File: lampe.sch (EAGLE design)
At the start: 29 parts, among them SW1 SWITCH, SW2 SWITCH, SW3 SWITCH, SW4 SWITCH, T3 LTR-4206, X1 USBPCB

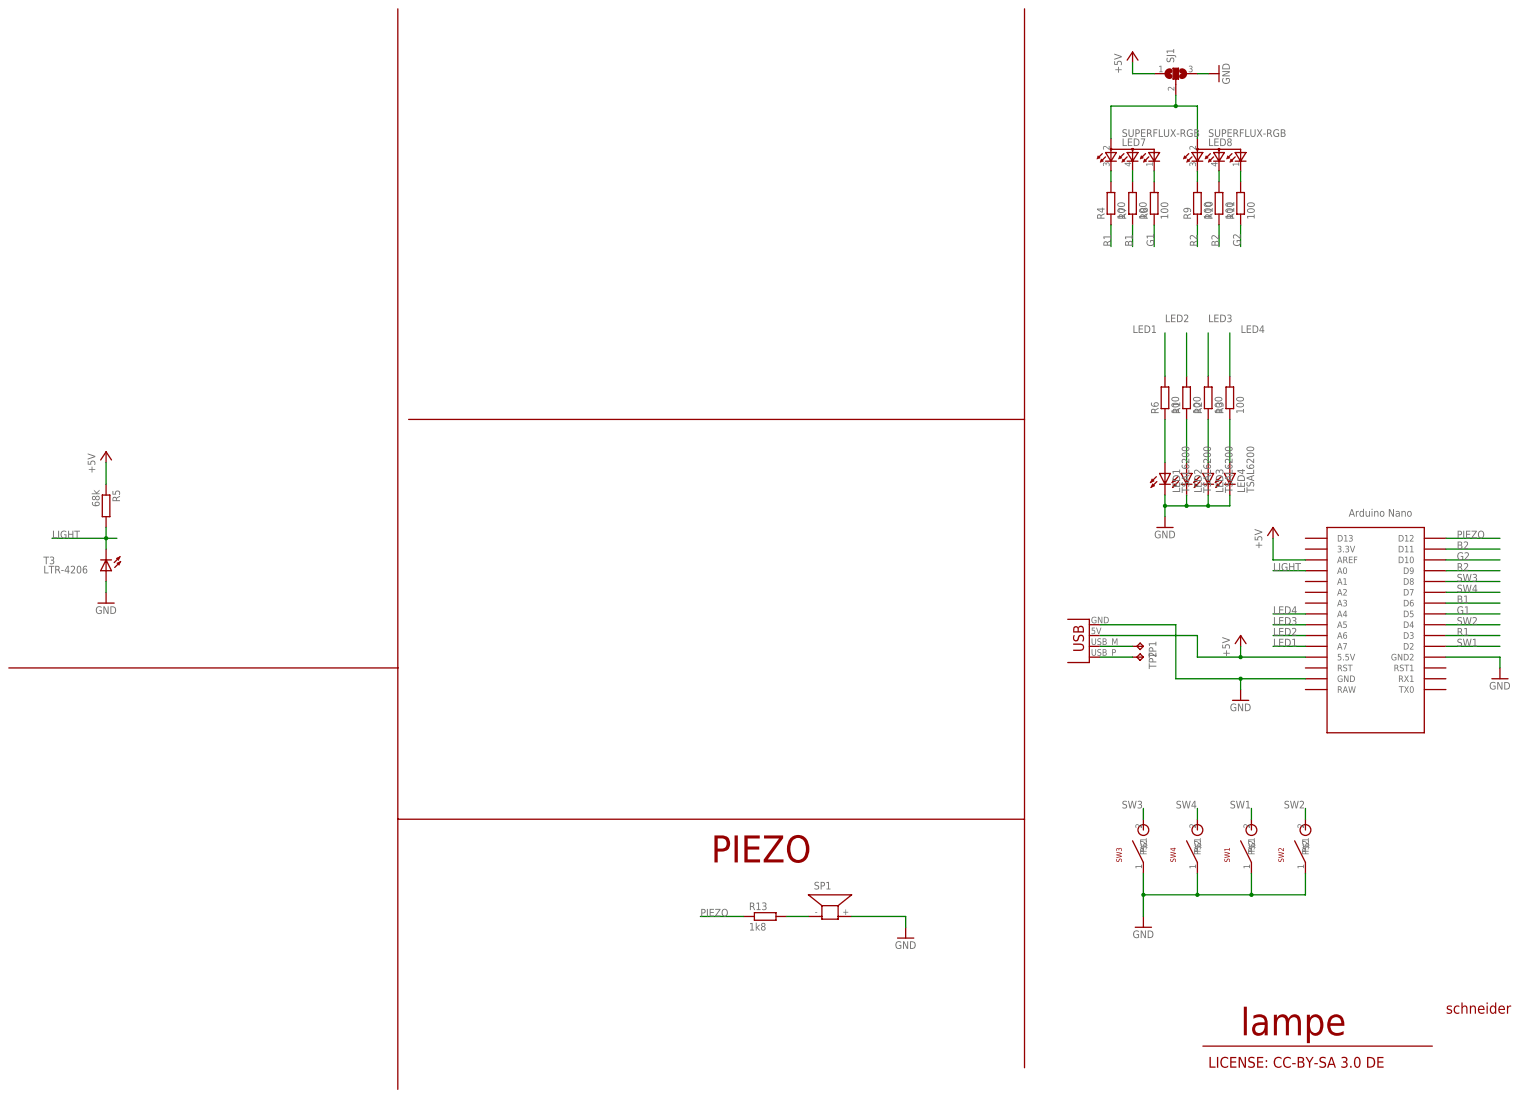
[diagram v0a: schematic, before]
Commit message: feat(lampe): Fix silk screen and some values
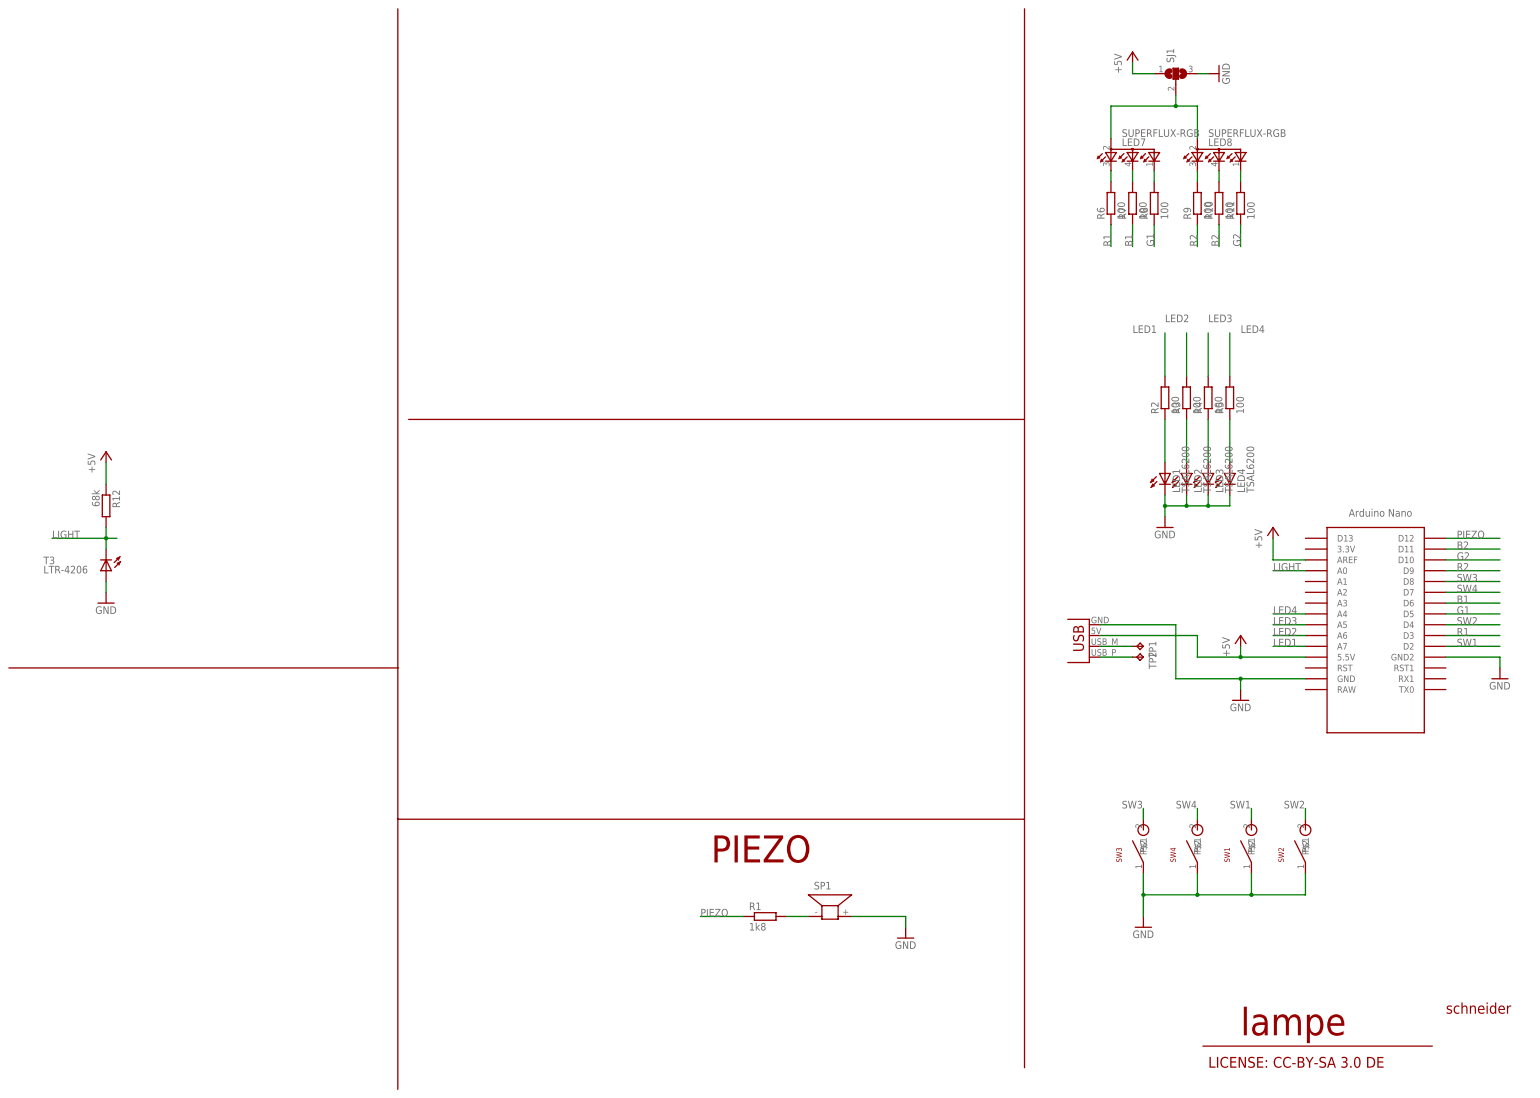
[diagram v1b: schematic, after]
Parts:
- removed R13: 1k8, rcl:R-EU_0207/7
- added R12: 68k, rcl:R-EU_0207/7
- R1: value 100 -> 1k8
- R5: value 68k -> 100
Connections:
- net +5V: now also R12.1; no longer R5.1
- net LED1: now also R2.2; no longer R6.2
- net LED2: now also R3.2; no longer R1.2
- net LED3: now also R4.2; no longer R2.2
- net LED4: now also R5.2; no longer R3.2
- net LIGHT: now also R12.2; no longer R5.2
- net N$1: now also R3.1; no longer R1.1
- net N$10: now also R5.1; no longer R3.1
- net N$17: now also R2.1; no longer R6.1
- net N$2: now also R6.2; no longer R4.2
- net N$29: now also R1.2; no longer R13.2
- net N$3: now also R4.1; no longer R2.1
- net PIEZO: now also R1.1; no longer R13.1
- net R1: now also R6.1; no longer R4.1
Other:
- moved on the sheet: R1, R2, R3, R4, R5, R6
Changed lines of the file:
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@@
 <parts>
 <part name="T3" library="led" deviceset="LED" device="3MM" value="LTR-4206"/>
-<part name="R5" library="rcl" deviceset="R-EU_" device="0207/7" value="68k"/>
+<part name="R12" library="rcl" deviceset="R-EU_" device="0207/7" value="68k"/>
 <part name="GND1" library="supply1" deviceset="GND" device=""/>
 <part name="GND6" library="supply1" deviceset="GND" device=""/>
@@
 <part name="GND10" library="supply1" deviceset="GND" device=""/>
 <part name="LED1" library="led" deviceset="LED" device="5MM" value="TSAL6200"/>
-<part name="R6" library="rcl" deviceset="R-EU_" device="0207/7" value="100"/>
-<part name="R13" library="rcl" deviceset="R-EU_" device="0207/7" value="1k8"/>
+<part name="R2" library="rcl" deviceset="R-EU_" device="0207/7" value="100"/>
+<part name="R1" library="rcl" deviceset="R-EU_" device="0207/7" value="1k8"/>
 <part name="GND13" library="supply1" deviceset="GND" device=""/>
 <part name="SW4" library="badge" deviceset="SWITCH" device="" value=""/>
@@
 <part name="SW1" library="badge" deviceset="SWITCH" device="" value=""/>
 <part name="SW2" library="badge" deviceset="SWITCH" device="" value=""/>
-<part name="R1" library="rcl" deviceset="R-EU_" device="0207/7" value="100"/>
-<part name="R2" library="rcl" deviceset="R-EU_" device="0207/7" value="100"/>
 <part name="R3" library="rcl" deviceset="R-EU_" device="0207/7" value="100"/>
 <part name="R4" library="rcl" deviceset="R-EU_" device="0207/7" value="100"/>
+<part name="R5" library="rcl" deviceset="R-EU_" device="0207/7" value="100"/>
+<part name="R6" library="rcl" deviceset="R-EU_" device="0207/7" value="100"/>
 <part name="R7" library="rcl" deviceset="R-EU_" device="0207/7" value="100"/>
 <part name="R8" library="rcl" deviceset="R-EU_" device="0207/7" value="100"/>
@@
 <attribute name="VALUE" x="15.748" y="123.825" size="1.778" layer="96"/>
 </instance>
-<instance part="R5" gate="G$1" x="30.48" y="139.7" rot="R270"/>
+<instance part="R12" gate="G$1" x="30.48" y="139.7" rot="R270"/>
 <instance part="GND1" gate="1" x="274.32" y="40.64"/>
 <instance part="GND6" gate="1" x="30.48" y="116.84"/>
@@
 <instance part="GND10" gate="1" x="218.44" y="38.1"/>
 <instance part="LED1" gate="G$1" x="279.4" y="147.32"/>
-<instance part="R6" gate="G$1" x="279.4" y="165.1" rot="R90"/>
-<instance part="R13" gate="G$1" x="185.42" y="43.18"/>
+<instance part="R2" gate="G$1" x="279.4" y="165.1" rot="R90"/>
+<instance part="R1" gate="G$1" x="185.42" y="43.18"/>
 <instance part="GND13" gate="1" x="279.4" y="134.62"/>
 <instance part="SW4" gate="G$1" x="287.02" y="58.42" rot="R90"/>
@@
 <instance part="SW1" gate="G$1" x="299.72" y="58.42" rot="R90"/>
 <instance part="SW2" gate="G$1" x="312.42" y="58.42" rot="R90"/>
-<instance part="R1" gate="G$1" x="284.48" y="165.1" rot="R90"/>
-<instance part="R2" gate="G$1" x="289.56" y="165.1" rot="R90"/>
-<instance part="R3" gate="G$1" x="294.64" y="165.1" rot="R90"/>
-<instance part="R4" gate="G$1" x="266.7" y="210.82" rot="R90"/>
+<instance part="R3" gate="G$1" x="284.48" y="165.1" rot="R90"/>
+<instance part="R4" gate="G$1" x="289.56" y="165.1" rot="R90"/>
+<instance part="R5" gate="G$1" x="294.64" y="165.1" rot="R90"/>
+<instance part="R6" gate="G$1" x="266.7" y="210.82" rot="R90"/>
 <instance part="R7" gate="G$1" x="271.78" y="210.82" rot="R90"/>
 <instance part="R8" gate="G$1" x="276.86" y="210.82" rot="R90"/>
@@
 <net name="N$29" class="0">
 <segment>
-<pinref part="R13" gate="G$1" pin="2"/>
+<pinref part="R1" gate="G$1" pin="2"/>
 <wire x1="190.5" y1="43.18" x2="195.58" y2="43.18" width="0.1524" layer="91"/>
 <pinref part="SP1" gate="G$1" pin="1"/>
@@
 <segment>
 <wire x1="279.4" y1="160.02" x2="279.4" y2="149.86" width="0.1524" layer="91"/>
-<pinref part="R6" gate="G$1" pin="1"/>
+<pinref part="R2" gate="G$1" pin="1"/>
 <pinref part="LED1" gate="G$1" pin="A"/>
 </segment>
@@
 <wire x1="180.34" y1="43.18" x2="170.18" y2="43.18" width="0.1524" layer="91"/>
 <label x="170.18" y="43.18" size="1.778" layer="95"/>
-<pinref part="R13" gate="G$1" pin="1"/>
+<pinref part="R1" gate="G$1" pin="1"/>
 </segment>
 <segment>
@@
 <wire x1="279.4" y1="170.18" x2="279.4" y2="180.34" width="0.1524" layer="91"/>
 <label x="271.78" y="180.34" size="1.778" layer="95"/>
-<pinref part="R6" gate="G$1" pin="2"/>
+<pinref part="R2" gate="G$1" pin="2"/>
 </segment>
 <segment>
@@
 <junction x="30.48" y="132.08"/>
 <label x="17.78" y="132.08" size="1.778" layer="95"/>
-<pinref part="R5" gate="G$1" pin="2"/>
+<pinref part="R12" gate="G$1" pin="2"/>
 <pinref part="T3" gate="G$1" pin="C"/>
 </segment>
@@
 <net name="N$2" class="0">
 <segment>
-<pinref part="R4" gate="G$1" pin="2"/>
+<pinref part="R6" gate="G$1" pin="2"/>
 <pinref part="LED7" gate="G$1" pin="CRED"/>
 <wire x1="266.7" y1="215.9" x2="266.7" y2="218.44" width="0.1524" layer="91"/>
@@
 <segment>
 <wire x1="30.48" y1="149.86" x2="30.48" y2="144.78" width="0.1524" layer="91"/>
-<pinref part="R5" gate="G$1" pin="1"/>
+<pinref part="R12" gate="G$1" pin="1"/>
 <pinref part="P+4" gate="1" pin="+5V"/>
 </segment>
@@
 <net name="R1" class="0">
 <segment>
-<pinref part="R4" gate="G$1" pin="1"/>
+<pinref part="R6" gate="G$1" pin="1"/>
 <wire x1="266.7" y1="205.74" x2="266.7" y2="200.66" width="0.1524" layer="91"/>
 <label x="266.7" y="200.66" size="1.778" layer="95" rot="R90"/>
@@
 <segment>
 <pinref part="LED2" gate="G$1" pin="A"/>
-<pinref part="R1" gate="G$1" pin="1"/>
+<pinref part="R3" gate="G$1" pin="1"/>
 <wire x1="284.48" y1="149.86" x2="284.48" y2="160.02" width="0.1524" layer="91"/>
 </segment>
@@
 <segment>
 <pinref part="LED3" gate="G$1" pin="A"/>
-<pinref part="R2" gate="G$1" pin="1"/>
+<pinref part="R4" gate="G$1" pin="1"/>
 <wire x1="289.56" y1="149.86" x2="289.56" y2="160.02" width="0.1524" layer="91"/>
 </segment>
@@
 <segment>
 <pinref part="LED4" gate="G$1" pin="A"/>
-<pinref part="R3" gate="G$1" pin="1"/>
+<pinref part="R5" gate="G$1" pin="1"/>
 <wire x1="294.64" y1="149.86" x2="294.64" y2="160.02" width="0.1524" layer="91"/>
 </segment>
@@
 <net name="LED2" class="0">
 <segment>
-<pinref part="R1" gate="G$1" pin="2"/>
+<pinref part="R3" gate="G$1" pin="2"/>
 <wire x1="284.48" y1="170.18" x2="284.48" y2="180.34" width="0.1524" layer="91"/>
 <label x="279.4" y="182.88" size="1.778" layer="95"/>
@@
 <net name="LED3" class="0">
 <segment>
-<pinref part="R2" gate="G$1" pin="2"/>
+<pinref part="R4" gate="G$1" pin="2"/>
 <wire x1="289.56" y1="170.18" x2="289.56" y2="180.34" width="0.1524" layer="91"/>
 <label x="289.56" y="182.88" size="1.778" layer="95"/>
@@
 <net name="LED4" class="0">
 <segment>
-<pinref part="R3" gate="G$1" pin="2"/>
+<pinref part="R5" gate="G$1" pin="2"/>
 <wire x1="294.64" y1="170.18" x2="294.64" y2="180.34" width="0.1524" layer="91"/>
 <label x="297.18" y="180.34" size="1.778" layer="95"/>
